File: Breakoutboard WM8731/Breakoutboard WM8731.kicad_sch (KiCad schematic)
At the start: 0 parts

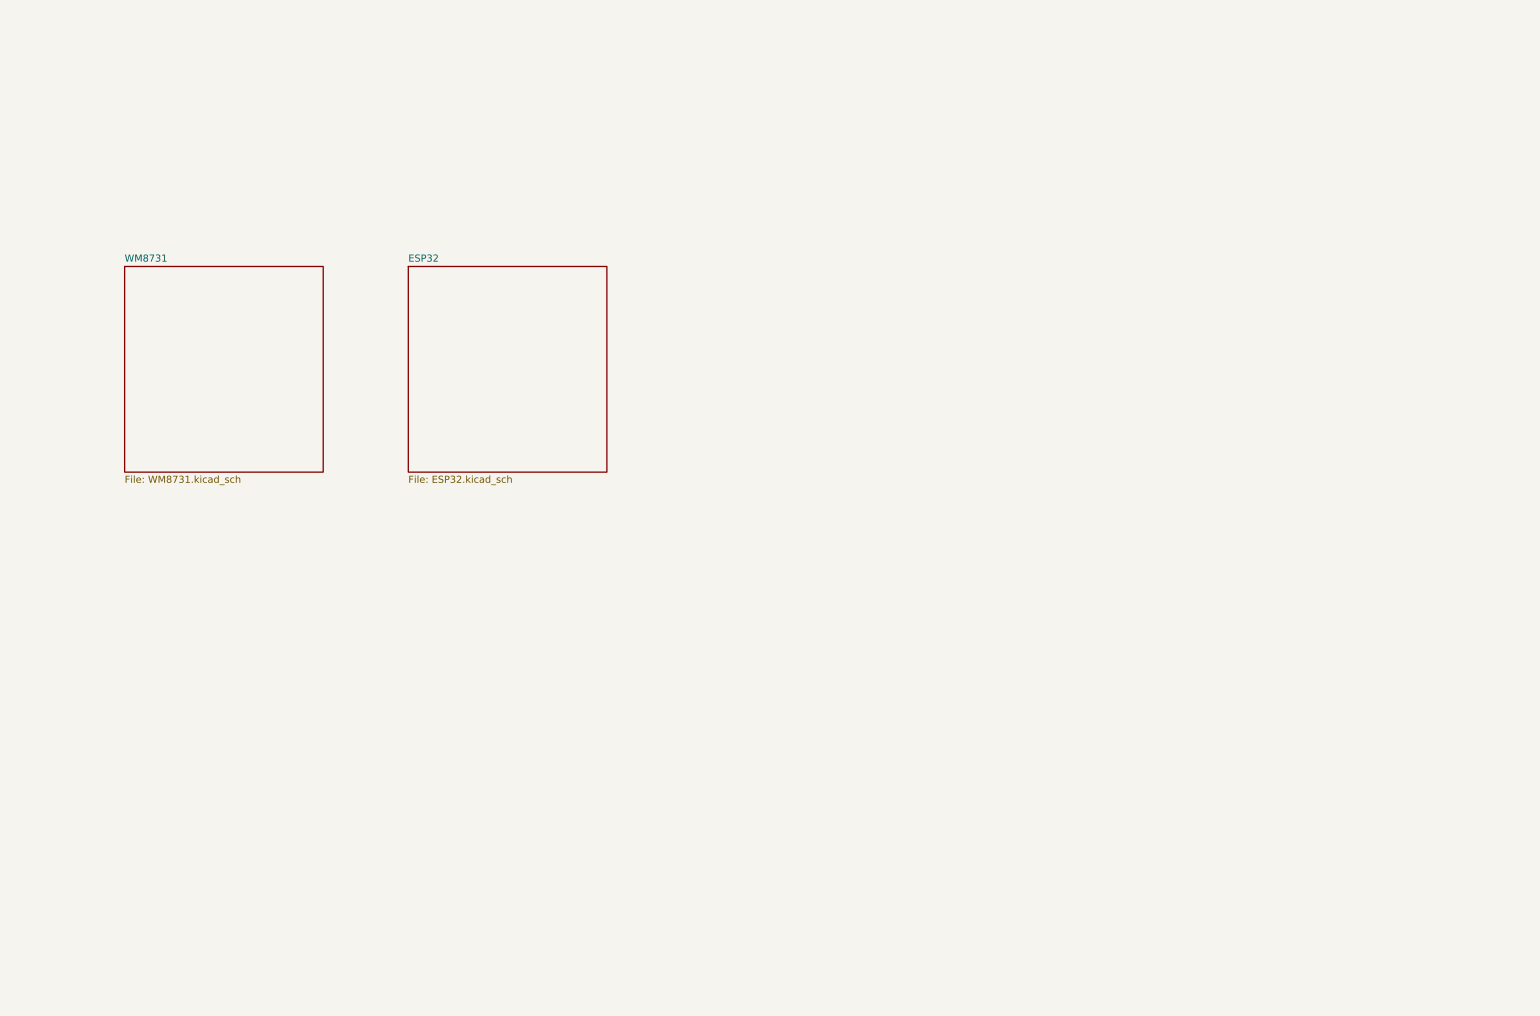
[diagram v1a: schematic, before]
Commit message: reworked power symbols and ESP32 schematic
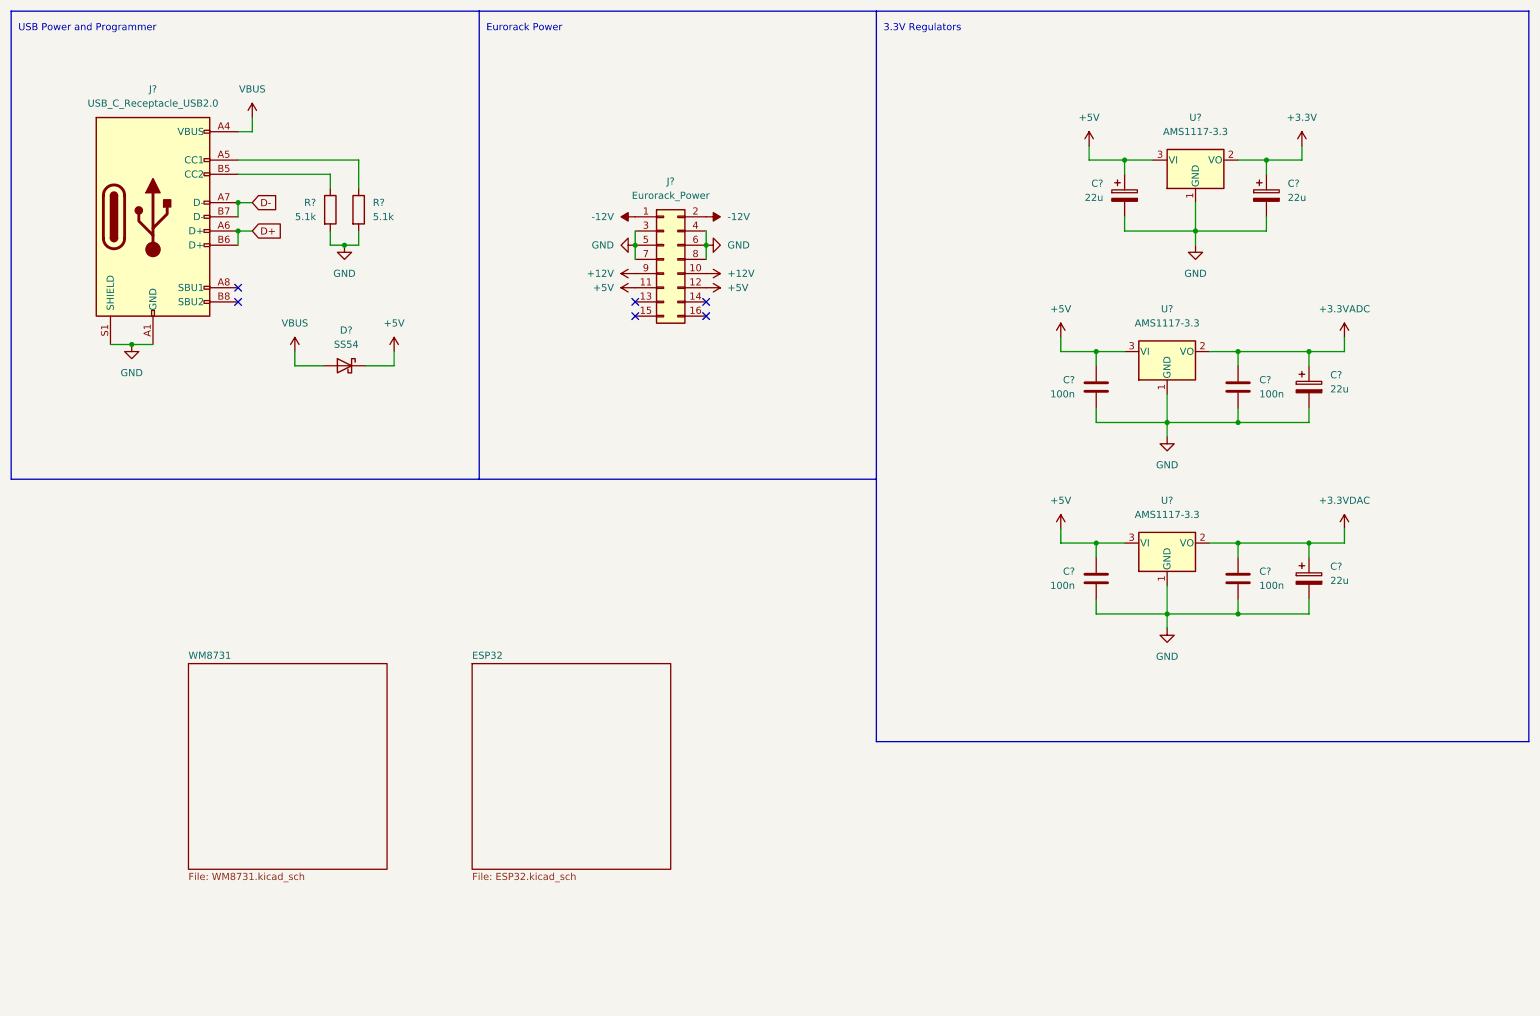
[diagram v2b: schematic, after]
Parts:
- added C? (x4): 100n, symbol Device:C
- added C? (x4): 22u, symbol Device:C_Polarized
- added D?: SS54, symbol Device:D_Schottky
- added J?: USB_C_Receptacle_USB2.0, symbol Connector:USB_C_Receptacle_USB2.0
- added J?: Eurorack_Power, symbol Connector_Generic:Conn_02x08_Odd_Even
- added R? (x2): 5.1k, symbol Device:R
- added U? (x3): AMS1117-3.3, Package_TO_SOT_SMD:SOT-223-3_TabPin2, symbol Regulator_Linear:AMS1117-3.3
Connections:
- new net: J?.A5 (CC1), R?.1
- new net: J?.B5 (CC2), R?.1
- new net +12V: J?.10 (Pin_10), J?.9 (Pin_9)
- new net +3.3VADC: C?.1, C?.1, U?.2 (VO)
- new net +3.3VDAC: C?.1, C?.1, U?.2 (VO)
- new net +3V3: C?.1, U?.2 (VO)
- new net +5V: C?.1, C?.1, C?.1, D?.1 (K), J?.11 (Pin_11), J?.12 (Pin_12), U?.3 (VI), U?.3 (VI), U?.3 (VI)
- new net -12V: J?.1 (Pin_1), J?.2 (Pin_2)
- new net D+: J?.A6 (D+), J?.B6 (D+)
- new net D-: J?.A7 (D-), J?.B7 (D-)
- new net GND: C?.2, C?.2, C?.2, C?.2, C?.2, C?.2, C?.2, C?.2, J?.3 (Pin_3), J?.4 (Pin_4), J?.5 (Pin_5), J?.6 (Pin_6), J?.7 (Pin_7), J?.8 (Pin_8), J?.A1 (GND), J?.A12 (GND), J?.B1 (GND), J?.B12 (GND), J?.S1 (SHIELD), R?.2, R?.2, U?.1 (GND), U?.1 (GND), U?.1 (GND)
- new net VBUS: D?.2 (A), J?.A4 (VBUS), J?.A9 (VBUS), J?.B4 (VBUS), J?.B9 (VBUS)
- no-connect marks 0 -> 6
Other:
- note added: "3.3V Regulators"
- note added: "Eurorack Power"
- note added: "USB Power and Programmer"

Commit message: added power status leds and 12V filtering
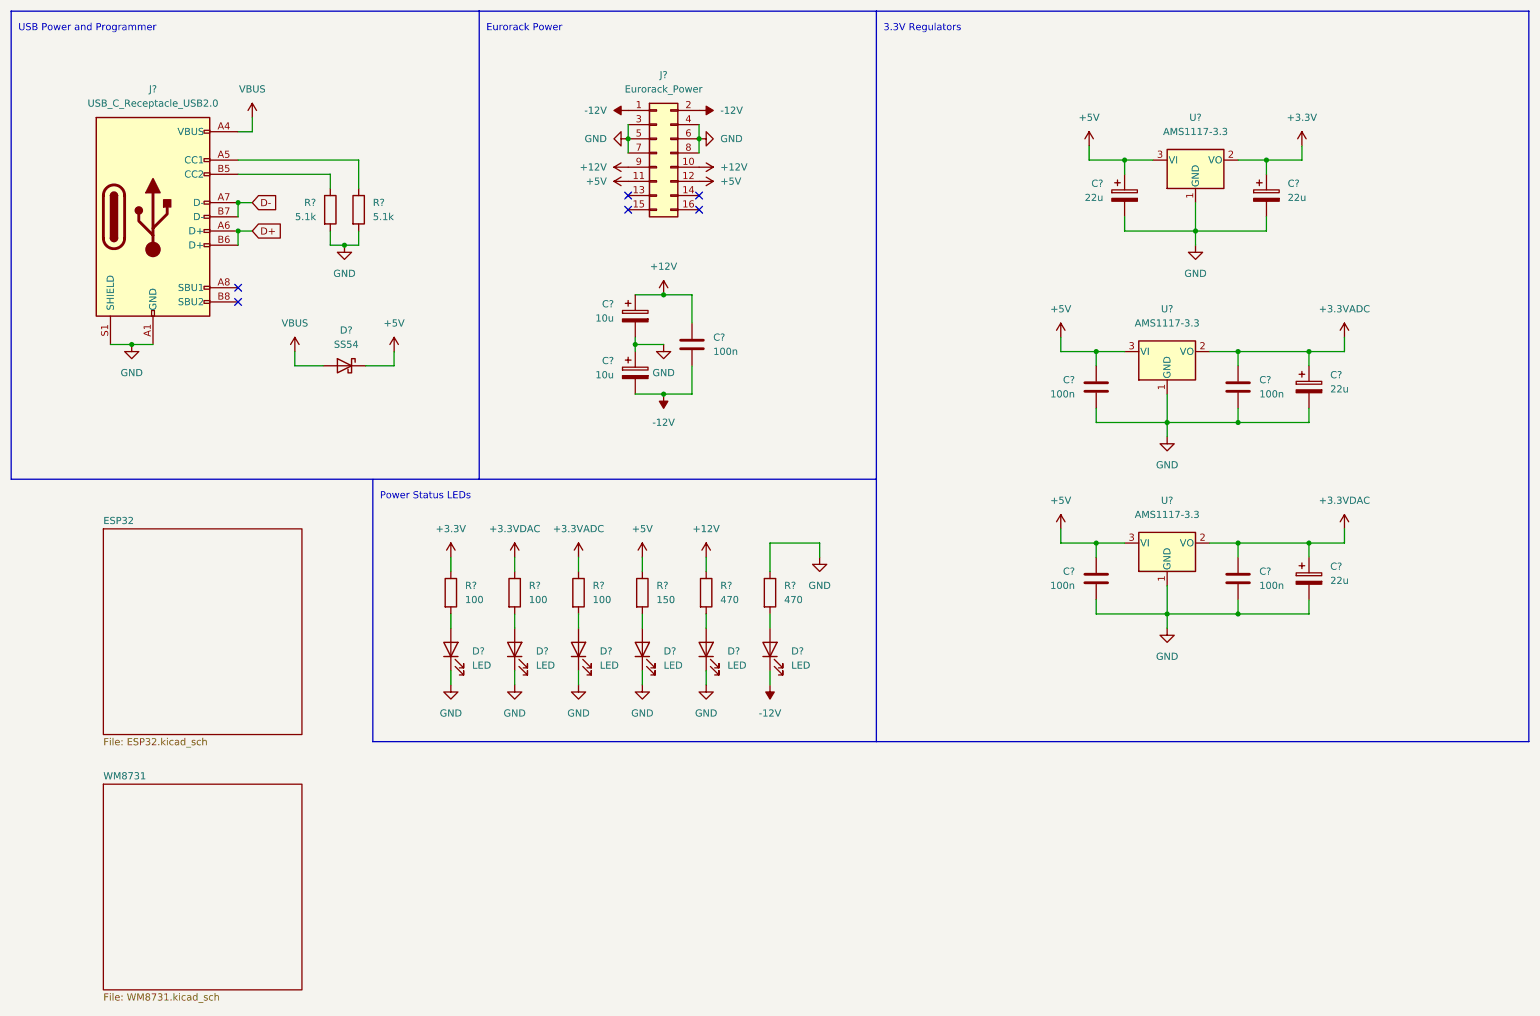
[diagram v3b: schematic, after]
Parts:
- added C? (x2): 10u, symbol Device:C_Polarized
- added C?: 100n, symbol Device:C
- added D? (x6): LED, symbol Device:LED
- added R? (x2): 470, symbol Device:R
- added R? (x3): 100, symbol Device:R
- added R?: 150, symbol Device:R
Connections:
- net +12V: now also C?.1, C?.1, R?.1
- net +3.3VADC: now also R?.1
- net +3.3VDAC: now also R?.1
- net +3V3: now also R?.1
- net +5V: now also R?.1
- net -12V: now also C?.2, C?.2, D?.1 (K)
- net GND: now also C?.1, C?.2, D?.1 (K), D?.1 (K), D?.1 (K), D?.1 (K), D?.1 (K), R?.1
- new net: D?.2 (A), R?.2 (x6)
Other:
- note added: "Power Status LEDs"
- moved on the sheet: J?
